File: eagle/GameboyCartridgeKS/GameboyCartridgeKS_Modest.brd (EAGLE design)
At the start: 49.3 x 48 mm, 20 parts, among them IC2 MEGA64-A, Y1 16MHz max

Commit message: Modest beta before wiring
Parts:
- added JOE: (no value), SparkFun-Passives:PAD-JUMPER-3-NO_YES_SILK
- added SCL, SCL1, SCL2, SCL3, SCL4, SDA: (no value), SparkFun-Passives:PAD.03X.05
- TP1, TP2, TP3, TP4, TP5, TP6: value TEST-POINT3X5 -> (none)
- moved D1 6.48 mm to (2.22, 20.4)
- moved JD1 6.36 mm to (2.22, 19.2)
- moved TP6 5.08 mm to (18.8, 24.7)
- moved TP1 1.09 mm to (48.3, 30.9)
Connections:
- removed net 10: U$1.10
- removed net 11: U$1.11
- removed net 12: U$1.12
- removed net 13: U$1.13
- removed net 14: U$1.14
- removed net 15: U$1.15
- removed net 16: U$1.16
- removed net 17: U$1.17
- removed net 18: U$1.18
- removed net 19: U$1.19
- removed net 20: U$1.20
- removed net 3: U$1.3
- removed net 30: U$1.30
- removed net 5: U$1.5
- removed net 6: U$1.6
- removed net 7: U$1.7
- removed net 8: U$1.8
- removed net 9: U$1.9
- new net !GB_CS: IC2.30, SCL4.P$1, U$1.5
- new net !GB_RD: IC2.29, JOE.3, SCL3.P$1, U$1.4
- new net !GB_RESET: IC2.31, U$1.30
- new net !GB_WR: IC2.28, SCL2.P$1, U$1.3
- new net GB_CLOCK: IC2.27, SCL1.P$1, U$1.2
- new net GB_MIC_IN: IC2.17, U$1.31
- new net N$1: IC2.26, SDA.P$1
- new net N$5: IC2.25, SCL.P$1
- new net N$7: IC2.14, JOE.1
- net !CE: now also IC2.13; no longer U$1.21
- net !OE: now also JOE.2; no longer U$1.4
- net !RESET: now also IC2.16
- net !WE: now also IC2.15; no longer U$1.31
- net ADDRESS0: now also IC2.61, U$1.6; no longer IC2.25
- net ADDRESS1: now also IC2.60, U$1.7; no longer IC2.26
- net ADDRESS10: now also U$1.16
- net ADDRESS11: now also U$1.17
- net ADDRESS12: now also U$1.18
- net ADDRESS13: now also U$1.19
- net ADDRESS14: now also U$1.20
- net ADDRESS15: now also U$1.21
- net ADDRESS2: now also IC2.59, U$1.8; no longer IC2.27
- net ADDRESS3: now also IC2.58, U$1.9; no longer IC2.28
- net ADDRESS4: now also IC2.57, U$1.10; no longer IC2.29
- net ADDRESS5: now also IC2.56, U$1.11; no longer IC2.30
- net ADDRESS6: now also IC2.55, U$1.12; no longer IC2.31
- net ADDRESS7: now also IC2.54, U$1.13; no longer IC2.32
- net ADDRESS8: now also U$1.14
- net ADDRESS9: now also U$1.15

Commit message: Minor edit
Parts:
- moved JOE 0.20 mm to (48.4, 26.7), turned to 270 degrees
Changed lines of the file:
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@@
 <element name="SCL3" library="SparkFun-Passives" package="PAD.03X.05" value="" x="6.7945" y="8.763"/>
 <element name="SCL4" library="SparkFun-Passives" package="PAD.03X.05" value="" x="8.1915" y="10.4775"/>
-<element name="JOE" library="SparkFun-Passives" package="PAD-JUMPER-3-NO_YES_SILK" value="" x="48.5775" y="26.6065" rot="R90"/>
+<element name="JOE" library="SparkFun-Passives" package="PAD-JUMPER-3-NO_YES_SILK" value="" x="48.387" y="26.67" rot="R270"/>
 </elements>
 <signals>
@@
 <wire x1="9.43" y1="26.49" x2="6.23" y2="42.09" width="0" layer="19" extent="1-1"/>
 <wire x1="18.78" y1="24.67" x2="9.43" y2="26.49" width="0" layer="19" extent="1-1"/>
-<wire x1="11.43" y1="12.97" x2="18.78" y2="24.67" width="0" layer="19" extent="1-1"/>
-<wire x1="6.35" y1="12.97" x2="11.43" y2="12.97" width="0" layer="19" extent="1-1"/>
 <wire x1="26.9" y1="21.59" x2="18.78" y2="24.67" width="0" layer="19" extent="1-1"/>
 <wire x1="36.63" y1="27.48" x2="26.9" y2="21.59" width="0" layer="19" extent="1-1"/>
+<wire x1="11.43" y1="12.97" x2="9.43" y2="26.49" width="0" layer="19" extent="1-1"/>
+<wire x1="6.35" y1="12.97" x2="11.43" y2="12.97" width="0" layer="19" extent="1-1"/>
 <wire x1="48.95" y1="4" x2="36.63" y2="27.48" width="0" layer="19" extent="1-1"/>
 </signal>
@@
 <contactref element="D1" pad="A"/>
 <contactref element="JD1" pad="1"/>
-<wire x1="2.2225" y1="18.727" x2="2.2225" y2="16.637" width="0" layer="19" extent="1-1"/>
+<wire x1="2.2225" y1="16.637" x2="2.2225" y2="18.727" width="0" layer="19" extent="1-1"/>
 <wire x1="2.05" y1="4" x2="2.2225" y2="16.637" width="0" layer="19" extent="1-1"/>
 </signal>
@@
 <contactref element="IC2" pad="30"/>
 <contactref element="SCL4" pad="P$1"/>
-<wire x1="8.25" y1="4" x2="15.83" y2="26.49" width="0" layer="19" extent="1-1"/>
-<wire x1="8.1915" y1="10.4775" x2="8.25" y2="4" width="0" layer="19" extent="1-1"/>
+<wire x1="8.1915" y1="10.4775" x2="15.83" y2="26.49" width="0" layer="19" extent="1-1"/>
+<wire x1="8.25" y1="4" x2="8.1915" y2="10.4775" width="0" layer="19" extent="1-1"/>
 </signal>
 <signal name="!GB_WR">
@@
 <contactref element="IC2" pad="28"/>
 <contactref element="SCL2" pad="P$1"/>
-<wire x1="5.25" y1="4" x2="14.23" y2="26.49" width="0" layer="19" extent="1-1"/>
-<wire x1="5.334" y1="10.3505" x2="5.25" y2="4" width="0" layer="19" extent="1-1"/>
+<wire x1="5.334" y1="10.3505" x2="14.23" y2="26.49" width="0" layer="19" extent="1-1"/>
+<wire x1="5.25" y1="4" x2="5.334" y2="10.3505" width="0" layer="19" extent="1-1"/>
 </signal>
 <signal name="22">
@@
 <contactref element="SCL3" pad="P$1"/>
 <contactref element="JOE" pad="3"/>
-<wire x1="6.75" y1="4" x2="15.03" y2="26.49" width="0" layer="19" extent="1-1"/>
-<wire x1="6.7945" y1="8.763" x2="6.75" y2="4" width="0" layer="19" extent="1-1"/>
-<wire x1="48.5775" y1="27.4193" x2="6.7945" y2="8.763" width="0" layer="19" extent="1-1"/>
+<wire x1="15.03" y1="26.49" x2="48.387" y2="25.8572" width="0" layer="19" extent="1-1"/>
+<wire x1="6.7945" y1="8.763" x2="15.03" y2="26.49" width="0" layer="19" extent="1-1"/>
+<wire x1="6.75" y1="4" x2="6.7945" y2="8.763" width="0" layer="19" extent="1-1"/>
 </signal>
 <signal name="!WE">
@@
 <contactref element="IC2" pad="27"/>
 <contactref element="SCL1" pad="P$1"/>
-<wire x1="3.75" y1="4" x2="13.43" y2="26.49" width="0" layer="19" extent="1-1"/>
-<wire x1="3.683" y1="8.9535" x2="3.75" y2="4" width="0" layer="19" extent="1-1"/>
+<wire x1="3.683" y1="8.9535" x2="13.43" y2="26.49" width="0" layer="19" extent="1-1"/>
+<wire x1="3.75" y1="4" x2="3.683" y2="8.9535" width="0" layer="19" extent="1-1"/>
 </signal>
 <signal name="N$1">
 <contactref element="IC2" pad="26"/>
 <contactref element="SDA" pad="P$1"/>
-<wire x1="16.51" y1="22.86" x2="12.63" y2="26.49" width="0" layer="19" extent="1-1"/>
+<wire x1="12.63" y1="26.49" x2="16.51" y2="22.86" width="0" layer="19" extent="1-1"/>
 </signal>
 <signal name="N$5">
@@
 <contactref element="TP2" pad="P$1"/>
 <contactref element="JOE" pad="2"/>
+<wire x1="48.387" y1="26.67" x2="48.301" y2="32.886" width="0" layer="19" extent="1-1"/>
 <wire x1="41.71" y1="32.56" x2="48.301" y2="32.886" width="0" layer="19" extent="1-1"/>
-<wire x1="48.5775" y1="26.6065" x2="41.71" y2="32.56" width="0" layer="19" extent="1-1"/>
 </signal>
 <signal name="N$7">
 <contactref element="JOE" pad="1"/>
 <contactref element="IC2" pad="14"/>
-<wire x1="48.5775" y1="25.7937" x2="3.63" y2="29.89" width="0" layer="19" extent="1-1"/>
+<wire x1="3.63" y1="29.89" x2="48.387" y2="27.4828" width="0" layer="19" extent="1-1"/>
 </signal>
 </signals>

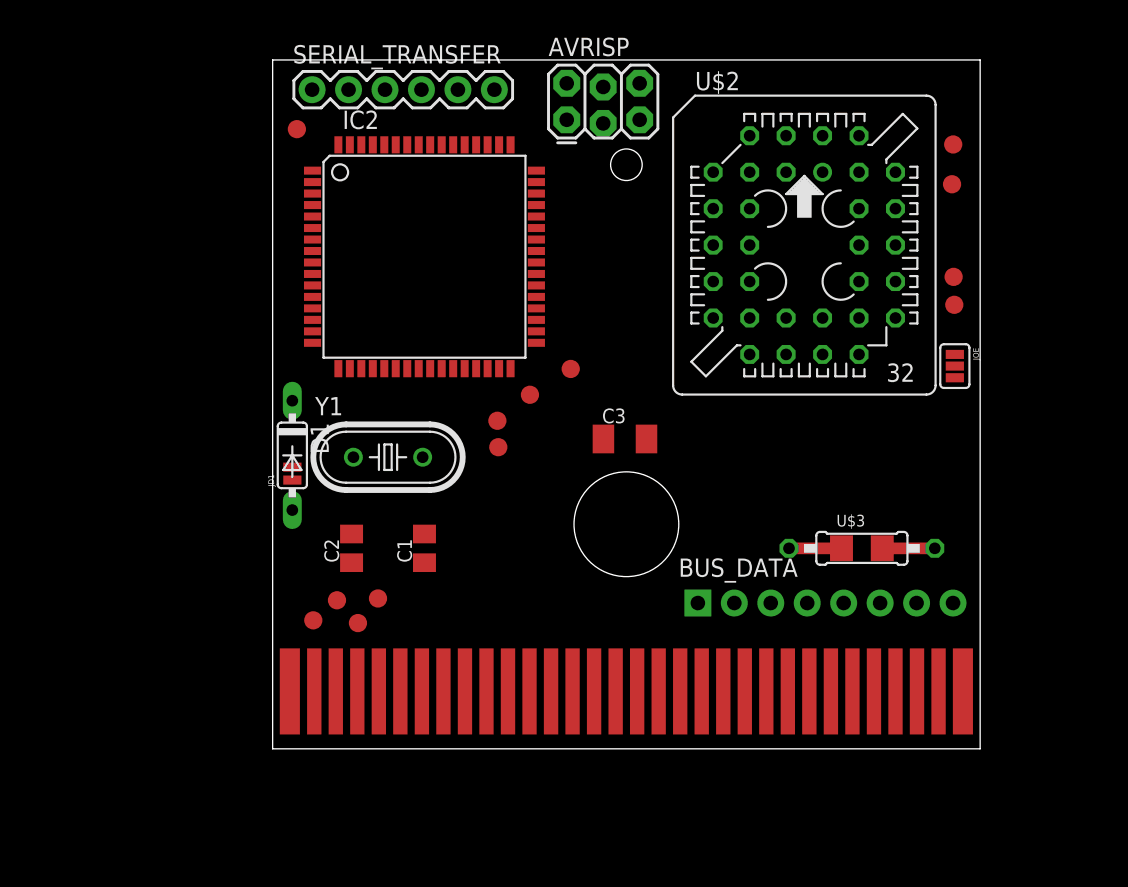
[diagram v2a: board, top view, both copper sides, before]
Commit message: Schema finished, TODO start final placement.
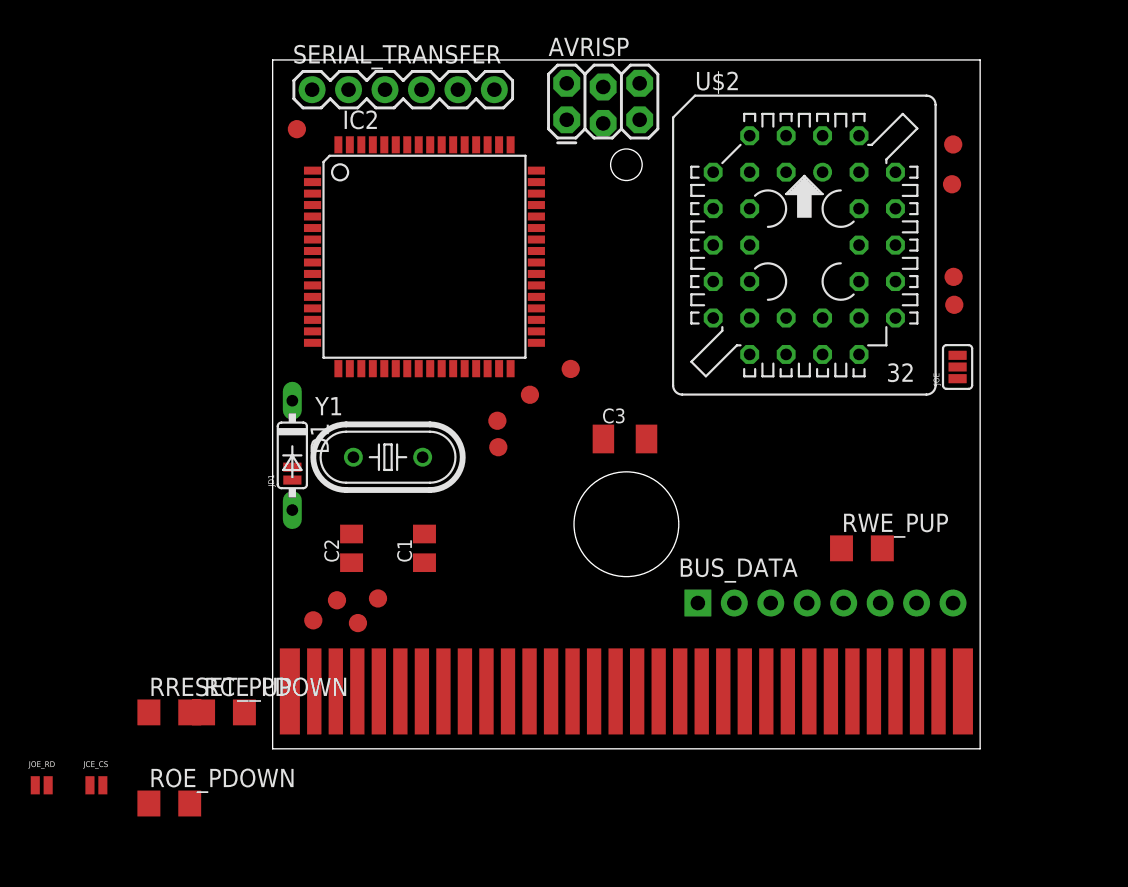
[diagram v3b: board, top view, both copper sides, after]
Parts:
- removed U$3: RESISTOR_COMBO1206, kalshagar:207-10_SMD_COMBO
- added JCE_CS, JOE_RD: (no value), SparkFun-Passives:PAD-JUMPER-2-NO_NO_SILK
- added RCE_PDOWN, ROE_PDOWN, RRESET_PUP, RWE_PUP: (no value), resistor:R1206
- moved JOE 0.20 mm to (48.6, 26.6), turned to 90 degrees
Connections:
- net !CE: now also JCE_CS.2, RCE_PDOWN.2
- net !GB_CS: now also JCE_CS.1
- net !GB_RD: now also JOE_RD.1
- net !OE: now also JOE_RD.2, ROE_PDOWN.2
- net !RESET: now also RRESET_PUP.1
- net !WE: now also RWE_PUP.1; no longer U$3.1, U$3.4
- net GND: now also RCE_PDOWN.1, ROE_PDOWN.1
- net VCC: now also RRESET_PUP.2, RWE_PUP.2; no longer U$3.2, U$3.3
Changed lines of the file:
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@@
 <element name="C1" library="resistor" package="C0805K" value="22pF" x="11.43" y="13.97" rot="R90"/>
 <element name="C2" library="resistor" package="C0805K" value="22pF" x="6.35" y="13.97" rot="R90"/>
-<element name="U$3" library="kalshagar" package="207-10_SMD_COMBO" value="RESISTOR_COMBO1206" x="41.91" y="13.97"/>
+<element name="RWE_PUP" library="resistor" package="R1206" value="" x="41.91" y="13.97"/>
 <element name="IC2" library="atmel" package="TQFP64" value="MEGA64-A" x="11.43" y="34.29">
 <attribute name="OC_NEWARK" value="01M6899" x="-6.35" y="54.61" size="1.778" layer="27" display="off"/>
@@
 <element name="SCL3" library="SparkFun-Passives" package="PAD.03X.05" value="" x="6.7945" y="8.763"/>
 <element name="SCL4" library="SparkFun-Passives" package="PAD.03X.05" value="" x="8.1915" y="10.4775"/>
-<element name="JOE" library="SparkFun-Passives" package="PAD-JUMPER-3-NO_YES_SILK" value="" x="48.387" y="26.67" rot="R270"/>
+<element name="JOE" library="SparkFun-Passives" package="PAD-JUMPER-3-NO_YES_SILK" value="" x="48.5775" y="26.6065" rot="R90"/>
+<element name="RCE_PDOWN" library="resistor" package="R1206" value="" x="-2.54" y="2.54"/>
+<element name="RRESET_PUP" library="resistor" package="R1206" value="" x="-6.35" y="2.54"/>
+<element name="ROE_PDOWN" library="resistor" package="R1206" value="" x="-6.35" y="-3.81"/>
+<element name="JCE_CS" library="SparkFun-Passives" package="PAD-JUMPER-2-NO_NO_SILK" value="" x="-11.43" y="-2.54"/>
+<element name="JOE_RD" library="SparkFun-Passives" package="PAD-JUMPER-2-NO_NO_SILK" value="" x="-15.24" y="-2.54"/>
 </elements>
 <signals>
@@
 <contactref element="SERIAL_TRANSFER" pad="1"/>
 <contactref element="C3" pad="2"/>
+<contactref element="RCE_PDOWN" pad="1"/>
+<contactref element="ROE_PDOWN" pad="1"/>
 <wire x1="14.23" y1="42.09" x2="26.4235" y2="46.372" width="0" layer="19" extent="1-1"/>
 <wire x1="6.23" y1="42.09" x2="14.23" y2="42.09" width="0" layer="19" extent="1-1"/>
@@
 <wire x1="11.43" y1="12.97" x2="9.43" y2="26.49" width="0" layer="19" extent="1-1"/>
 <wire x1="6.35" y1="12.97" x2="11.43" y2="12.97" width="0" layer="19" extent="1-1"/>
+<wire x1="-3.962" y1="2.54" x2="6.35" y2="12.97" width="0" layer="19" extent="1-1"/>
+<wire x1="-7.772" y1="-3.81" x2="-3.962" y2="2.54" width="0" layer="19" extent="1-1"/>
 <wire x1="48.95" y1="4" x2="36.63" y2="27.48" width="0" layer="19" extent="1-1"/>
 </signal>
@@
 <contactref element="D1" pad="A"/>
 <contactref element="JD1" pad="1"/>
-<wire x1="2.2225" y1="16.637" x2="2.2225" y2="18.727" width="0" layer="19" extent="1-1"/>
+<wire x1="2.2225" y1="18.727" x2="2.2225" y2="16.637" width="0" layer="19" extent="1-1"/>
 <wire x1="2.05" y1="4" x2="2.2225" y2="16.637" width="0" layer="19" extent="1-1"/>
 </signal>
@@
 <contactref element="IC2" pad="30"/>
 <contactref element="SCL4" pad="P$1"/>
+<contactref element="JCE_CS" pad="1"/>
 <wire x1="8.1915" y1="10.4775" x2="15.83" y2="26.49" width="0" layer="19" extent="1-1"/>
 <wire x1="8.25" y1="4" x2="8.1915" y2="10.4775" width="0" layer="19" extent="1-1"/>
+<wire x1="-11.88" y1="-2.54" x2="8.25" y2="4" width="0" layer="19" extent="1-1"/>
 </signal>
 <signal name="!GB_WR">
@@
 <contactref element="IC2" pad="28"/>
 <contactref element="SCL2" pad="P$1"/>
-<wire x1="5.334" y1="10.3505" x2="14.23" y2="26.49" width="0" layer="19" extent="1-1"/>
-<wire x1="5.25" y1="4" x2="5.334" y2="10.3505" width="0" layer="19" extent="1-1"/>
+<wire x1="5.25" y1="4" x2="14.23" y2="26.49" width="0" layer="19" extent="1-1"/>
+<wire x1="5.334" y1="10.3505" x2="5.25" y2="4" width="0" layer="19" extent="1-1"/>
 </signal>
 <signal name="22">
@@
 <contactref element="U$2" pad="32"/>
 <contactref element="AVRISP" pad="2"/>
-<contactref element="U$3" pad="2"/>
-<contactref element="U$3" pad="3"/>
+<contactref element="RWE_PUP" pad="2"/>
 <contactref element="IC2" pad="62"/>
 <contactref element="IC2" pad="64"/>
@@
 <contactref element="D1" pad="C"/>
 <contactref element="JD1" pad="2"/>
+<contactref element="RRESET_PUP" pad="2"/>
 <wire x1="21.3435" y1="46.372" x2="39.17" y2="42.72" width="0" layer="19" extent="1-1"/>
 <wire x1="15.03" y1="42.09" x2="21.3435" y2="46.372" width="0" layer="19" extent="1-1"/>
@@
 <wire x1="21.62" y1="26.47" x2="8.63" y2="26.49" width="0" layer="19" extent="1-1"/>
 <wire x1="23.9" y1="21.59" x2="21.62" y2="26.47" width="0" layer="19" extent="1-1"/>
+<wire x1="-4.928" y1="2.54" x2="2.2225" y2="19.627" width="0" layer="19" extent="1-1"/>
 <wire x1="43.18" y1="13.97" x2="23.9" y2="21.59" width="0" layer="19" extent="1-1"/>
 <wire x1="43.332" y1="13.97" x2="43.18" y2="13.97" width="0" layer="19" extent="1-1"/>
@@
 <contactref element="TP1" pad="P$1"/>
 <contactref element="IC2" pad="13"/>
+<contactref element="RCE_PDOWN" pad="2"/>
+<contactref element="JCE_CS" pad="2"/>
 <wire x1="41.71" y1="30.02" x2="48.347" y2="30.9395" width="0" layer="19" extent="1-1"/>
 <wire x1="3.63" y1="30.69" x2="41.71" y2="30.02" width="0" layer="19" extent="1-1"/>
+<wire x1="-1.118" y1="2.54" x2="3.63" y2="30.69" width="0" layer="19" extent="1-1"/>
+<wire x1="-10.98" y1="-2.54" x2="-1.118" y2="2.54" width="0" layer="19" extent="1-1"/>
 </signal>
 <signal name="!GB_RD">
@@
 <contactref element="SCL3" pad="P$1"/>
 <contactref element="JOE" pad="3"/>
-<wire x1="15.03" y1="26.49" x2="48.387" y2="25.8572" width="0" layer="19" extent="1-1"/>
+<contactref element="JOE_RD" pad="1"/>
+<wire x1="15.03" y1="26.49" x2="48.5775" y2="27.4193" width="0" layer="19" extent="1-1"/>
 <wire x1="6.7945" y1="8.763" x2="15.03" y2="26.49" width="0" layer="19" extent="1-1"/>
 <wire x1="6.75" y1="4" x2="6.7945" y2="8.763" width="0" layer="19" extent="1-1"/>
+<wire x1="-15.69" y1="-2.54" x2="6.75" y2="4" width="0" layer="19" extent="1-1"/>
 </signal>
 <signal name="!WE">
 <contactref element="TP3" pad="P$1"/>
 <contactref element="U$2" pad="31"/>
-<contactref element="U$3" pad="4"/>
-<contactref element="U$3" pad="1"/>
 <contactref element="IC2" pad="15"/>
+<contactref element="RWE_PUP" pad="1"/>
 <wire x1="41.71" y1="40.18" x2="48.1915" y2="39.341" width="0" layer="19" extent="1-1"/>
 <wire x1="40.488" y1="13.97" x2="41.71" y2="40.18" width="0" layer="19" extent="1-1"/>
-<wire x1="40.64" y1="13.97" x2="40.488" y2="13.97" width="0" layer="19" extent="1-1"/>
-<wire x1="3.63" y1="29.09" x2="36.83" y2="13.97" width="0" layer="19" extent="1-1"/>
+<wire x1="3.63" y1="29.09" x2="41.71" y2="40.18" width="0" layer="19" extent="1-1"/>
 </signal>
 <signal name="!RESET">
@@
 <contactref element="TP4" pad="P$1"/>
 <contactref element="IC2" pad="16"/>
+<contactref element="RRESET_PUP" pad="1"/>
 <wire x1="39.17" y1="40.18" x2="48.2725" y2="42.113" width="0" layer="19" extent="1-1"/>
 <wire x1="3.63" y1="28.29" x2="39.17" y2="40.18" width="0" layer="19" extent="1-1"/>
+<wire x1="-7.772" y1="2.54" x2="3.63" y2="28.29" width="0" layer="19" extent="1-1"/>
 </signal>
 <signal name="MISO_TX">
@@
 <contactref element="IC2" pad="27"/>
 <contactref element="SCL1" pad="P$1"/>
-<wire x1="3.683" y1="8.9535" x2="13.43" y2="26.49" width="0" layer="19" extent="1-1"/>
-<wire x1="3.75" y1="4" x2="3.683" y2="8.9535" width="0" layer="19" extent="1-1"/>
+<wire x1="3.75" y1="4" x2="13.43" y2="26.49" width="0" layer="19" extent="1-1"/>
+<wire x1="3.683" y1="8.9535" x2="3.75" y2="4" width="0" layer="19" extent="1-1"/>
 </signal>
 <signal name="N$1">
 <contactref element="IC2" pad="26"/>
 <contactref element="SDA" pad="P$1"/>
-<wire x1="12.63" y1="26.49" x2="16.51" y2="22.86" width="0" layer="19" extent="1-1"/>
+<wire x1="16.51" y1="22.86" x2="12.63" y2="26.49" width="0" layer="19" extent="1-1"/>
 </signal>
 <signal name="N$5">
@@
 <contactref element="TP2" pad="P$1"/>
 <contactref element="JOE" pad="2"/>
-<wire x1="48.387" y1="26.67" x2="48.301" y2="32.886" width="0" layer="19" extent="1-1"/>
+<contactref element="ROE_PDOWN" pad="2"/>
+<contactref element="JOE_RD" pad="2"/>
+<wire x1="48.5775" y1="26.6065" x2="48.301" y2="32.886" width="0" layer="19" extent="1-1"/>
 <wire x1="41.71" y1="32.56" x2="48.301" y2="32.886" width="0" layer="19" extent="1-1"/>
+<wire x1="-4.928" y1="-3.81" x2="41.71" y2="32.56" width="0" layer="19" extent="1-1"/>
+<wire x1="-14.79" y1="-2.54" x2="-4.928" y2="-3.81" width="0" layer="19" extent="1-1"/>
 </signal>
 <signal name="N$7">
 <contactref element="JOE" pad="1"/>
 <contactref element="IC2" pad="14"/>
-<wire x1="3.63" y1="29.89" x2="48.387" y2="27.4828" width="0" layer="19" extent="1-1"/>
+<wire x1="48.5775" y1="25.7937" x2="3.63" y2="29.89" width="0" layer="19" extent="1-1"/>
 </signal>
 </signals>

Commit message: Placement beta before routing
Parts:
- added PEN1, PEN2, PEN3, PEN4: TEST-POINT3X5, SparkFun-Passives:PAD.03X.05
- moved JOE_RD 63.2 mm to (43.2, 21.6), turned to 270 degrees
- moved JCE_CS 62.0 mm to (45.7, 21.6), turned to 270 degrees
- moved RRESET_PUP 56.7 mm to (48.3, 17.8), turned to 270 degrees
- moved ROE_PDOWN 54.0 mm to (43.2, 17.8), turned to 90 degrees
- moved RCE_PDOWN 50.6 mm to (45.7, 17.8), turned to 90 degrees
- moved C3 25.0 mm to (2.54, 11.4), turned to 90 degrees
- moved C1 5.24 mm to (6.35, 15.2), turned to 180 degrees
- moved C2 5.24 mm to (11.4, 15.2), turned to 0 degrees
- moved RWE_PUP 4.02 mm to (40.6, 17.8), turned to 270 degrees
- moved JOE 3.81 mm to (48.6, 22.8)
- moved TP6 1.27 mm to (19.5, 23.7)
- moved SCL1 1.27 mm to (4.95, 8.95)
- moved SCL2 1.27 mm to (6.60, 10.4)
- moved SCL3 1.27 mm to (8.06, 8.76)
- moved SCL4 1.27 mm to (9.46, 10.5)
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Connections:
- net GND: now also PEN1.P$1, PEN2.P$1
- net VCC: now also PEN3.P$1, PEN4.P$1
